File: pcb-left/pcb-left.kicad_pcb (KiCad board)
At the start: 2 copper layers, 124.8 x 104.5 mm, 43 parts, among them J1 BAT, U1 xiao-ble

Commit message: WIP Update switch spacing to choc
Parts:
- moved DL1 266.9 mm to (251.9, 226.9)
- moved DL10 266.9 mm to (327.9, 235.0)
- moved DL12 266.9 mm to (270.9, 249.2)
- moved DL13 266.9 mm to (289.9, 243.1)
- moved DL14 266.9 mm to (308.9, 249.2)
- moved DL15 266.9 mm to (327.9, 254.0)
- moved DL16 266.9 mm to (308.9, 274.1)
- moved DL17 266.9 mm to (331.3, 274.9)
- moved DL2 266.9 mm to (270.9, 211.2)
- moved DL3 266.9 mm to (289.9, 205.1)
- moved DL4 266.9 mm to (308.9, 211.2)
- moved DL5 266.9 mm to (327.9, 216.0)
- moved DL6 266.9 mm to (251.9, 245.9)
- moved DL7 266.9 mm to (270.9, 230.2)
- moved DL8 266.9 mm to (289.9, 224.1)
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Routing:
- net COL0_L: track 58.2 -> 97.2 mm
- net ROW2_L: track 142.4 -> 122.8 mm
- net ROW1_L: track 124.0 -> 104.5 mm
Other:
- board size 124.8 x 104.5 mm -> 120.4 x 101.3 mm

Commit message: Tracks
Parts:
- moved bottomleft 355.8 mm to (33.4, 103.9)
- moved topleft 315.6 mm to (55.4, 32.9)
- moved DL15 283.1 mm to (108.0, 75.8)
- moved DL10 281.9 mm to (108.0, 58.7)
- moved DL16 281.7 mm to (90.0, 96.8)
- moved J1 281.6 mm to (76.0, 88.0)
- moved DL14 281.2 mm to (90.0, 72.8)
- moved DL17 281.0 mm to (112.9, 97.9), turned to -111 degrees
- moved DL5 280.6 mm to (108.0, 41.8)
- moved DL9 280.0 mm to (90.0, 55.8)
- moved DL18 279.8 mm to (133.5, 107.5), turned to -132 degrees
- moved DL12 279.5 mm to (54.0, 73.0)
- moved DL11 279.5 mm to (36.0, 87.5)
- moved DL13 279.1 mm to (72.0, 68.8)
- moved DL4 278.5 mm to (90.0, 39.0)
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- renumbered REF** to bottomleft, REF** to bottomright, REF** to topleft, REF** to topright
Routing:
- net GND_L: track 0.00 -> 189.4 mm, vias 46 -> 0
- net COL0_L: track 97.2 -> 52.6 mm
- net COL3_L: track 163.1 -> 145.2 mm, vias 1 -> 2
- net COL4_L: track 184.3 -> 166.8 mm
- net ROW0_L: track 90.7 -> 76.6 mm, vias 2 -> 0
- net VBAT_L: track 74.4 -> 84.6 mm, vias 0 -> 1
- net ROW2_L: track 122.8 -> 113.8 mm, vias 8 -> 5
- net COL2_L: track 128.4 -> 119.5 mm
- net ROW3_L: track 165.3 -> 157.8 mm, vias 2 -> 3
- net COL1_L: track 62.0 -> 56.9 mm
- net ROW1_L: track 104.5 -> 101.3 mm, vias 8 -> 4
- net RESET_L: track 89.3 -> 87.9 mm
- net Net-(DL18-A): track 8.38 -> 7.44 mm
- net Net-(DL5-A): track 8.31 -> 7.46 mm
- net Net-(DL15-A): track 8.31 -> 7.46 mm
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- removed copper zone on B.Cu, net GND_L
- removed copper zone on F.Cu, net GND_L
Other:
- board text removed: "XIAO nRF52840"

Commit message: Fixings
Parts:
- moved bottomright 7.15 mm to (121.5, 93.0)
- moved topleft 1.74 mm to (53.8, 32.5)
- moved bottomleft 1.09 mm to (32.5, 104.5)
- moved topright 0.50 mm to (127.5, 32.5)
- moved RSW1 0.20 mm to (115.6, 33.7)
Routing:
- net ROW0_L: track 76.6 -> 82.7 mm
- net ROW2_L: track 113.8 -> 117.4 mm
- net ROW1_L: track 101.3 -> 104.6 mm
- net GND_L: track 189.4 -> 189.0 mm, vias 0 -> 1
- net VBAT_L: track 84.6 -> 84.9 mm, vias 1 -> 0
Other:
- outline, holes or cut-outs redrawn
- board text removed: "BATTERY"

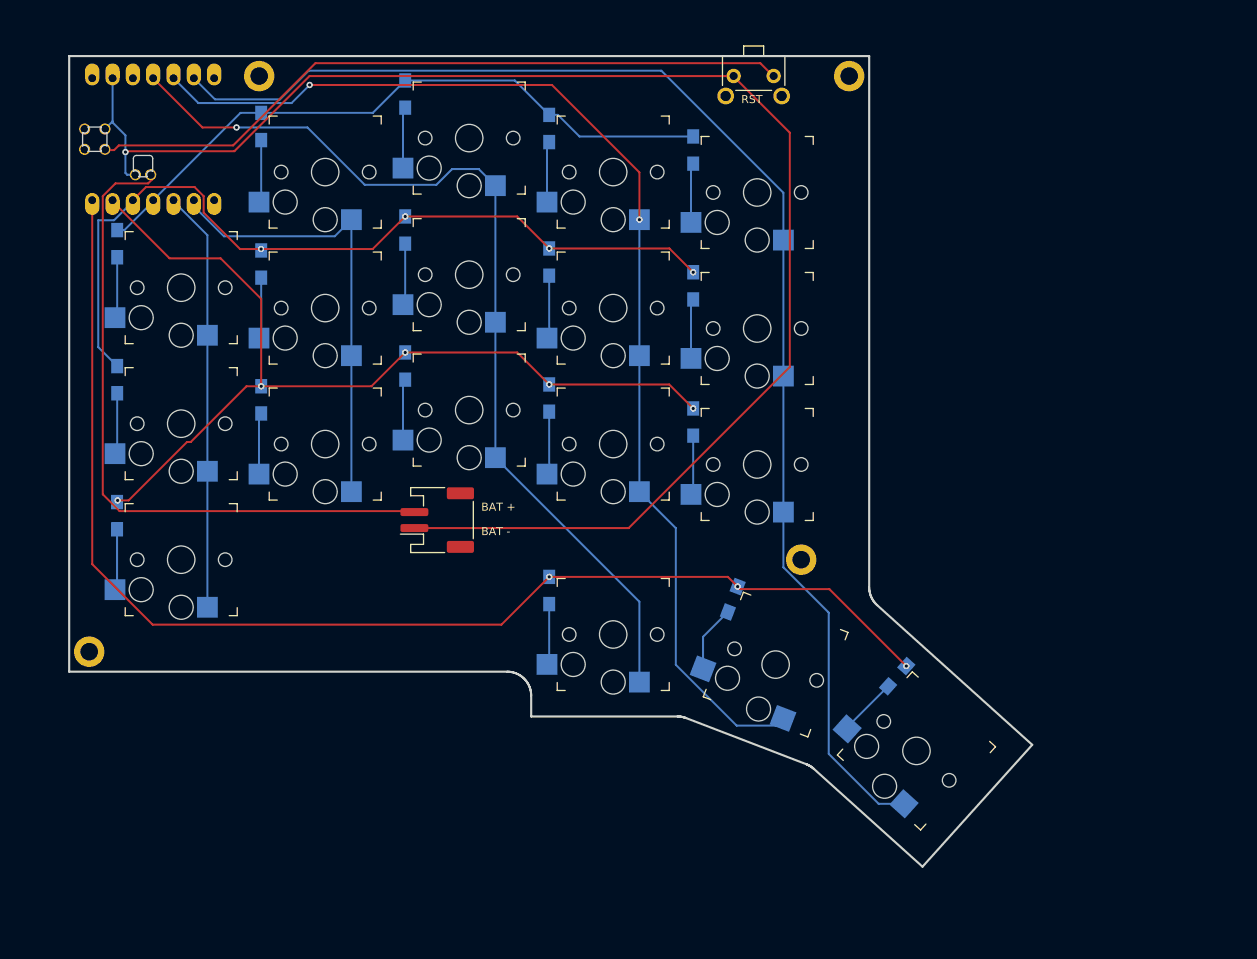
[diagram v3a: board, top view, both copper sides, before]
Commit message: Left Done
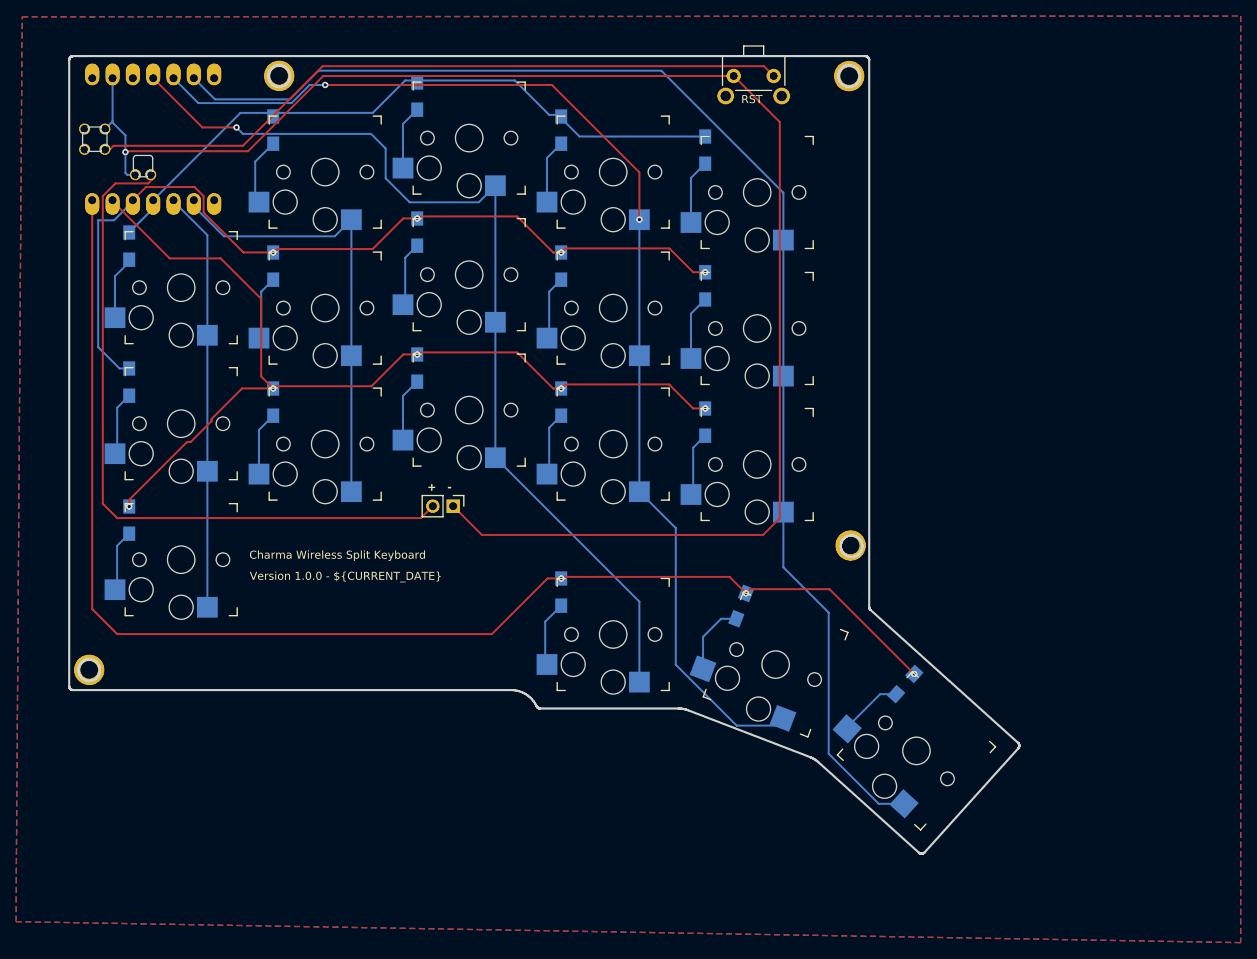
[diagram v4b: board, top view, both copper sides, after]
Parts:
- J1: footprint Connector_JST:JST_PH_S2B-PH-SM4-TB_1x02-1MP_P2.00mm_Horizontal -> Connector_PinHeader_2.54mm:PinHeader_1x02_P2.54mm_Vertical
- moved bottomright 6.43 mm to (127.7, 91.2)
- moved J1 2.65 mm to (78.0, 86.3), turned to -90 degrees
- moved topleft 2.50 mm to (56.2, 32.5)
- moved bottomleft 2.27 mm to (32.5, 106.7)
- moved DL11 1.62 mm to (37.5, 88.0)
- moved DL14 1.58 mm to (91.5, 73.2)
- moved DL9 1.58 mm to (91.5, 56.2)
- moved DL2 1.57 mm to (55.5, 39.2)
- moved DL1 1.53 mm to (37.5, 53.8)
- moved DL6 1.53 mm to (37.5, 70.8)
- moved DL12 1.53 mm to (55.5, 73.2)
- moved DL13 1.52 mm to (73.5, 69.0)
- moved DL3 1.52 mm to (73.5, 35.0)
- moved DL7 1.52 mm to (55.5, 56.2)
- moved DL8 1.52 mm to (73.5, 52.0)
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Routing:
- net GND_L: track 189.0 -> 195.3 mm
- net ROW3_L: track 157.5 -> 163.6 mm
- net VBAT_L: track 84.9 -> 88.5 mm
- net ROW1_L: track 104.6 -> 108.1 mm
- net COL2_L: track 119.5 -> 121.7 mm
- net ROW2_L: track 117.4 -> 119.4 mm
- net COL3_L: track 145.3 -> 144.1 mm
- net COL1_L: track 56.9 -> 56.1 mm
- net Net-(DL17-A): track 8.39 -> 9.10 mm
- net Net-(DL5-A): track 7.46 -> 8.09 mm
- net Net-(DL10-A): track 7.49 -> 8.11 mm
- added copper zone on B.Cu, net (none)
- added copper zone on F.Cu, net (none)
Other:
- board size 120.4 x 101.3 mm -> 118.8 x 99.7 mm
- board text added: "${TITLE}"
- board text added: "+"
- board text added: "-"
- board text added: "Version ${REVISION} - ${CURRENT_DATE}"
- board text removed: "BAT +"
- board text removed: "BAT -"

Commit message: PCB v1
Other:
- outline, holes or cut-outs redrawn

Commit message: Long overdue commit!
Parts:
- moved bottomright 0.25 mm to (127.5, 91.0)
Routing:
- net COL3_L: track 144.1 -> 143.4 mm
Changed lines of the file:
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@@
 	(footprint "MountingHole:MountingHole_2.2mm_M2_DIN965_Pad"
 		(layer "F.Cu")
-		(at 32.5 106.725)
+		(at 32.5 106.7)
 		(descr "Mounting Hole 2.2mm, M2, DIN965")
 		(tags "mounting hole 2.2mm m2 din965")
@@
 	(footprint "MountingHole:MountingHole_2.2mm_M2_DIN965_Pad"
 		(layer "F.Cu")
-		(at 56.25 32.475)
+		(at 56.25 32.5)
 		(descr "Mounting Hole 2.2mm, M2, DIN965")
 		(tags "mounting hole 2.2mm m2 din965")
@@
 	(footprint "MountingHole:MountingHole_2.2mm_M2_DIN965_Pad"
 		(layer "F.Cu")
-		(at 127.68 91.18)
+		(at 127.5 91)
 		(descr "Mounting Hole 2.2mm, M2, DIN965")
 		(tags "mounting hole 2.2mm m2 din965")
@@
 			(justify left bottom)
 		)
-		(render_cache "Version 1.0.0 - 2024-12-14" 0
+		(render_cache "Version 1.0.0 - 2024-12-16" 0
 			(polygon
 				(pts
@@
 			(polygon
 				(pts
-					(xy 69.78912 95.044842) (xy 69.917103 95.044842) (xy 69.917103 95.216789) (xy 69.78912 95.216789)
-					(xy 69.78912 95.42) (xy 69.586399 95.42) (xy 69.586399 95.216789) (xy 69.151646 95.216789) (xy 69.151646 95.044842)
-					(xy 69.362672 95.044842) (xy 69.586399 95.044842) (xy 69.586399 94.696552) (xy 69.583712 94.696552)
-					(xy 69.362672 95.044842) (xy 69.151646 95.044842) (xy 69.151646 95.039225) (xy 69.558311 94.419581)
-					(xy 69.78912 94.419581)
+					(xy 69.521674 94.788632) (xy 69.55538 94.781793) (xy 69.590551 94.779106) (xy 69.641521 94.78261)
+					(xy 69.692708 94.794312) (xy 69.718534 94.804019) (xy 69.762744 94.827244) (xy 69.804044 94.858926)
+					(xy 69.817208 94.871919) (xy 69.849392 94.912571) (xy 69.872998 94.955761) (xy 69.880467 94.973768)
+					(xy 69.895016 95.022843) (xy 69.902147 95.074418) (xy 69.902937 95.099064) (xy 69.899532 95.149752)
+					(xy 69.888049 95.201163) (xy 69.874117 95.237062) (xy 69.849513 95.280819) (xy 69.818933 95.319768)
+					(xy 69.795226 95.343063) (xy 69.755247 95.373403) (xy 69.710047 95.398109) (xy 69.677013 95.411451)
+					(xy 69.629096 95.425218) (xy 69.579044 95.43327) (xy 69.531688 95.435631) (xy 69.478779 95.432716)
+					(xy 69.428524 95.423971) (xy 69.385143 95.410963) (xy 69.337023 95.389576) (xy 69.29378 95.362419)
+					(xy 69.267662 95.341109) (xy 69.233246 95.304747) (xy 69.204739 95.26344) (xy 69.189016 95.233154)
+					(xy 69.171453 95.183981) (xy 69.162475 95.135225) (xy 69.160195 95.092714) (xy 69.160241 95.091737)
+					(xy 69.371221 95.091737) (xy 69.378517 95.142878) (xy 69.402693 95.189387) (xy 69.415429 95.203845)
+					(xy 69.456061 95.232468) (xy 69.505722 95.246498) (xy 69.531688 95.248053) (xy 69.581514 95.241836)
+					(xy 69.626809 95.22107) (xy 69.647459 95.203845) (xy 69.67624 95.163898) (xy 69.690349 95.116292)
+					(xy 69.691912 95.091737) (xy 69.684575 95.040637) (xy 69.660265 94.994261) (xy 69.647459 94.979874)
+					(xy 69.607026 94.951093) (xy 69.557563 94.936984) (xy 69.531688 94.935422) (xy 69.48168 94.941673)
+					(xy 69.436185 94.962553) (xy 69.415429 94.979874) (xy 69.386806 95.019663) (xy 69.372775 95.067191)
+					(xy 69.371221 95.091737) (xy 69.160241 95.091737) (xy 69.162637 95.041301) (xy 69.169965 94.994528)
+					(xy 69.183162 94.946143) (xy 69.196099 94.910753) (xy 69.217222 94.865059) (xy 69.233956 94.835282)
+					(xy 69.260749 94.791668) (xy 69.279874 94.761032) (xy 69.497739 94.419581) (xy 69.75517 94.419581)
 				)
 			)
@@
 	)
 	(segment
-		(start 105.825 89)
-		(end 105.825 106.078267)
+		(start 108.500095 89)
+		(end 120.590596 101.090501)
 		(width 0.25)
 		(layer "B.Cu")
@@
 	)
 	(segment
-		(start 105.825 106.078267)
-		(end 113.439282 113.692549)
+		(start 101.275 84.45)
+		(end 101.275 67.45)
 		(width 0.25)
 		(layer "B.Cu")
@@
 	)
 	(segment
-		(start 101.275 84.45)
-		(end 101.275 67.45)
+		(start 120.590596 111.426891)
+		(end 119.226283 112.791204)
 		(width 0.25)
 		(layer "B.Cu")
@@
 	)
 	(segment
-		(start 113.439282 113.692549)
-		(end 118.324938 113.692549)
+		(start 101.275 84.45)
+		(end 105.825 89)
 		(width 0.25)
 		(layer "B.Cu")
@@
 	)
 	(segment
-		(start 101.275 84.45)
-		(end 105.825 89)
+		(start 105.825 89)
+		(end 108.500095 89)
 		(width 0.25)
 		(layer "B.Cu")
@@
 	)
 	(segment
+		(start 120.590596 101.090501)
+		(end 120.590596 111.426891)
+		(width 0.25)
+		(layer "B.Cu")
+		(net 29)
+	)
+	(segment
 		(start 62 33.612)
 		(end 60.055 33.612)
@@
 		(min_thickness 0.25)
 		(filled_areas_thickness no)
-		(fill
+		(fill yes
 			(thermal_gap 0.5)
 			(thermal_bridge_width 0.5)
